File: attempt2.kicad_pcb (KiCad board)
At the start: 4 copper layers, 88.5 x 54.4 mm, 60 parts, among them J1 Conn_ARM_JTAG_SWD_10, J4 USB_C_Receptacle_USB2.0_14P, J5 SIM_Card, SW1 SW_Push, SW4 SW_Push, U3 MCP73831T-2ACI_OT, U4 NRF9151-LACA-R7, U5 MAX2686LEWS_, U7 CP2102N-A02-GQFN24R

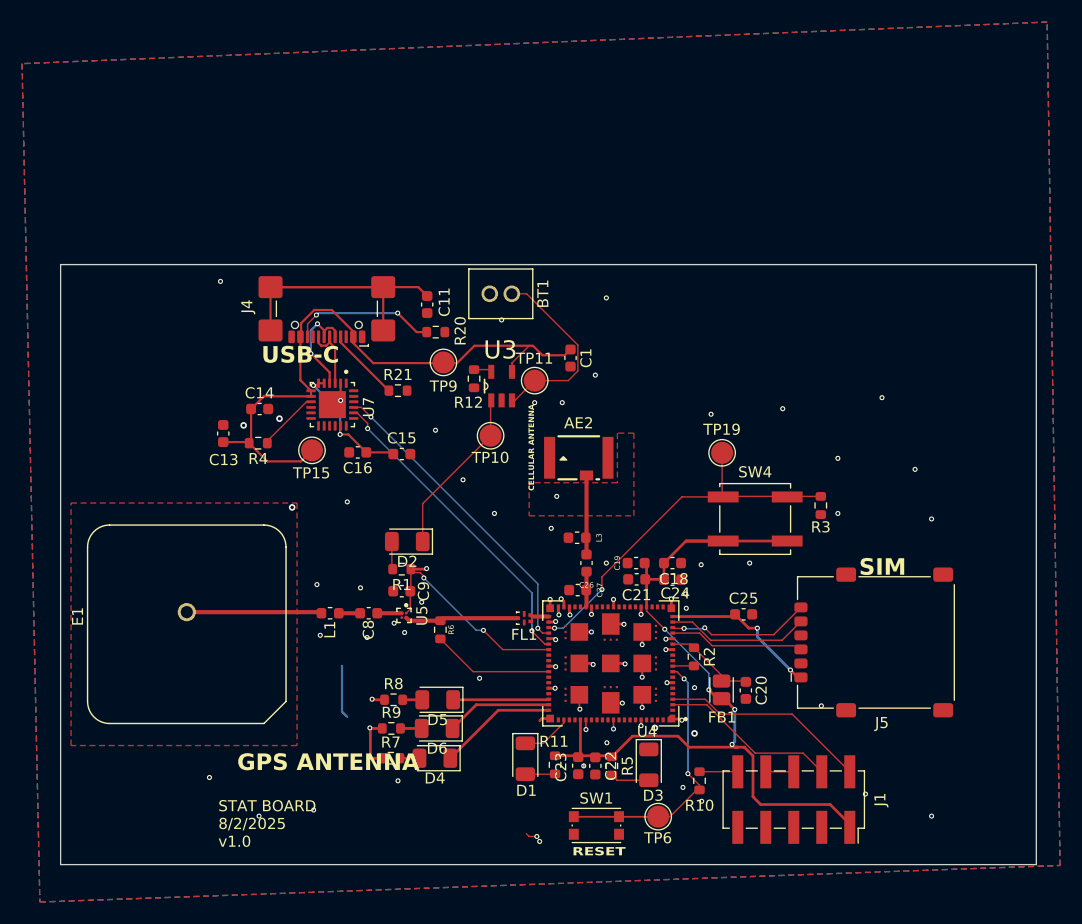
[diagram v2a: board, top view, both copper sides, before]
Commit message: moved some ground pins
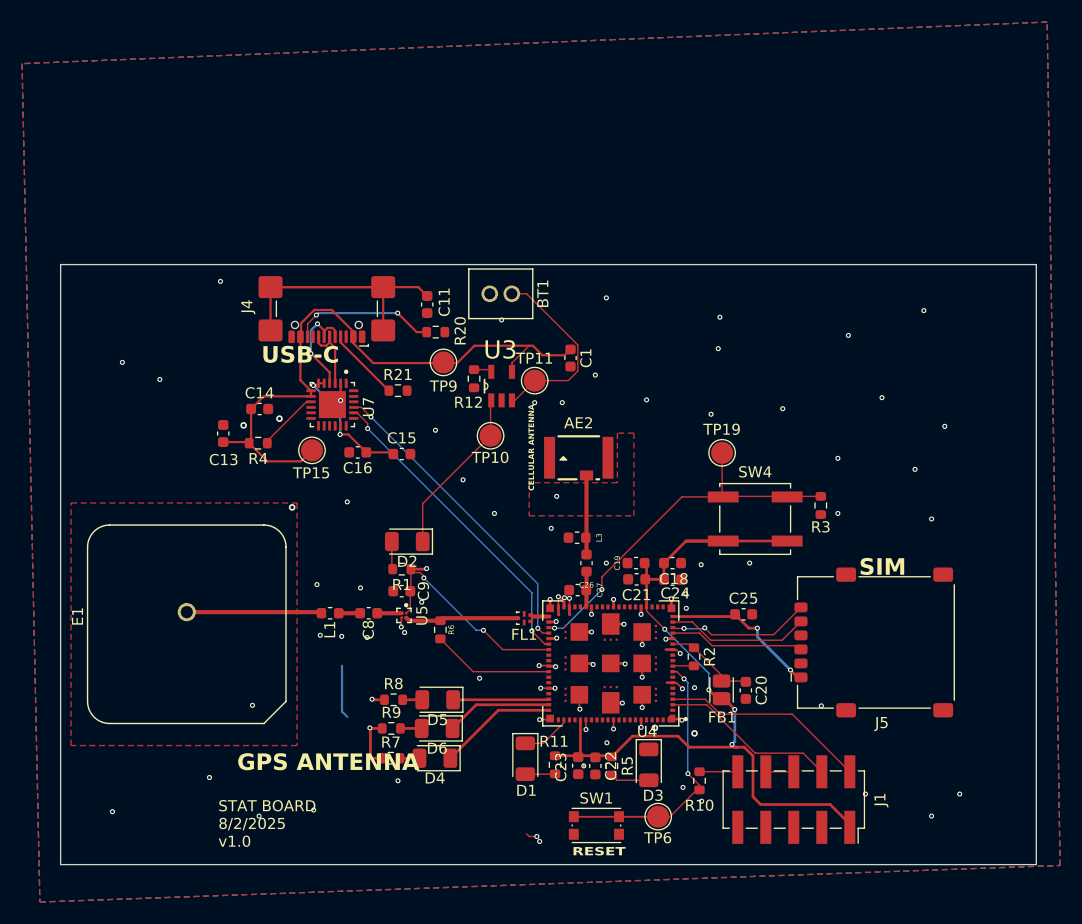
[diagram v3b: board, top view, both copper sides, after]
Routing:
- net GND: track 34.4 -> 43.7 mm, vias 80 -> 95
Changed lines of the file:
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@@
-	)
-	(segment
-		(start 132.15 128.15)
-		(end 131.95 128.35)
-		(width 0.25)
-		(layer "F.Cu")
-		(net 1)
 	)
 	(segment
@@
 	)
 	(segment
+		(start 132.675 120.85)
+		(end 133.5 120.85)
+		(width 0.15)
+		(layer "F.Cu")
+		(net 1)
+	)
+	(segment
+		(start 143.925 124.9)
+		(end 144.35 124.9)
+		(width 0.15)
+		(layer "F.Cu")
+		(net 1)
+	)
+	(segment
 		(start 135.55 120.3)
 		(end 136.65 120.3)
@@
 	)
 	(segment
+		(start 132.775 128.25)
+		(end 131.95 128.25)
+		(width 0.15)
+		(layer "F.Cu")
+		(net 1)
+	)
+	(segment
 		(start 132.775 120.9)
 		(end 133.3 120.9)
@@
 	)
 	(segment
+		(start 141.15 128.125)
+		(end 141.15 128.95)
+		(width 0.15)
+		(layer "F.Cu")
+		(net 1)
+	)
+	(segment
 		(start 136.7 123.15)
 		(end 136.8 123.25)
@@
 	)
 	(segment
+		(start 144.35 124.9)
+		(end 144.9 125.45)
+		(width 0.15)
+		(layer "F.Cu")
+		(net 1)
+	)
+	(segment
 		(start 113.525 99.675)
 		(end 113.9 99.3)
 		(width 0.2)
+		(layer "F.Cu")
+		(net 1)
+	)
+	(segment
+		(start 144.35 121.9)
+		(end 144.7 122.25)
+		(width 0.15)
 		(layer "F.Cu")
 		(net 1)
@@
 	)
 	(segment
+		(start 133.65 117.925)
+		(end 133.65 117.1)
+		(width 0.15)
+		(layer "F.Cu")
+		(net 1)
+	)
+	(segment
+		(start 132.625 119.35)
+		(end 133.45 119.35)
+		(width 0.15)
+		(layer "F.Cu")
+		(net 1)
+	)
+	(segment
 		(start 138.4 123.15)
 		(end 139.65 123.15)
@@
 	)
 	(segment
+		(start 132.725 123.35)
+		(end 131.9 123.35)
+		(width 0.15)
+		(layer "F.Cu")
+		(net 1)
+	)
+	(segment
 		(start 135.55 123.15)
 		(end 136.7 123.15)
@@
 		(end 133.4 121)
 		(width 0.25)
+		(layer "F.Cu")
+		(net 1)
+	)
+	(segment
+		(start 134.2 118.025)
+		(end 134.2 117.2)
+		(width 0.15)
 		(layer "F.Cu")
 		(net 1)
@@
 	)
 	(segment
+		(start 132.875 125.4)
+		(end 132.05 125.4)
+		(width 0.15)
+		(layer "F.Cu")
+		(net 1)
+	)
+	(segment
 		(start 133.65 118.025)
 		(end 133.65 118.7)
@@
 		(end 139.575 119.575)
 		(width 0.25)
+		(layer "F.Cu")
+		(net 1)
+	)
+	(segment
+		(start 119.4 119.025)
+		(end 119.4 119.85)
+		(width 0.15)
 		(layer "F.Cu")
 		(net 1)
@@
 	)
 	(segment
+		(start 143.975 121.9)
+		(end 144.35 121.9)
+		(width 0.15)
+		(layer "F.Cu")
+		(net 1)
+	)
+	(segment
 		(start 138.4 126.725)
 		(end 139.425 126.725)
@@
 	)
 	(segment
+		(start 134.65 118.075)
+		(end 134.65 117.25)
+		(width 0.15)
+		(layer "F.Cu")
+		(net 1)
+	)
+	(segment
 		(start 139.425 126.725)
 		(end 139.45 126.75)
@@
 	)
 	(segment
-		(start 132.9 128.15)
-		(end 132.15 128.15)
-		(width 0.25)
-		(layer "F.Cu")
-		(net 1)
-	)
-	(segment
 		(start 133.35 119.4)
 		(end 133.4 119.35)
@@
 	)
 	(via
-		(at 141.15 128.8)
-		(size 0.4572)
-		(drill 0.254)
-		(layers "F.Cu" "B.Cu")
+		(at 148.15 94.6)
+		(size 0.4572)
+		(drill 0.254)
+		(layers "F.Cu" "B.Cu")
+		(free yes)
+		(net 1)
+	)
+	(via
+		(at 168.7 101.65)
+		(size 0.4572)
+		(drill 0.254)
+		(layers "F.Cu" "B.Cu")
+		(free yes)
 		(net 1)
 	)
@@
 	)
 	(via
+		(at 132.05 125.4)
+		(size 0.4572)
+		(drill 0.254)
+		(layers "F.Cu" "B.Cu")
+		(net 1)
+	)
+	(via
+		(at 119.4 119.85)
+		(size 0.4572)
+		(drill 0.254)
+		(layers "F.Cu" "B.Cu")
+		(net 1)
+	)
+	(via
+		(at 144.9 125.45)
+		(size 0.4572)
+		(drill 0.254)
+		(layers "F.Cu" "B.Cu")
+		(net 1)
+	)
+	(via
 		(at 146.65 135.65)
 		(size 0.4572)
@@
 	)
 	(via
-		(at 133.4 119.35)
-		(size 0.4572)
-		(drill 0.254)
-		(layers "F.Cu" "B.Cu")
-		(net 1)
-	)
-	(via
-		(at 143.4 121.9)
-		(size 0.4572)
-		(drill 0.254)
-		(layers "F.Cu" "B.Cu")
-		(net 1)
-	)
-	(via
 		(at 143.9 117.3)
 		(size 0.4572)
@@
 	)
 	(via
-		(at 133.4 121)
+		(at 141.15 128.95)
+		(size 0.4572)
+		(drill 0.254)
+		(layers "F.Cu" "B.Cu")
+		(net 1)
+	)
+	(via
+		(at 133.45 119.35)
 		(size 0.4572)
 		(drill 0.254)
@@
 	)
 	(via
+		(at 134.2 117.2)
+		(size 0.4572)
+		(drill 0.254)
+		(layers "F.Cu" "B.Cu")
+		(net 1)
+	)
+	(via
 		(at 132.9 117.35)
 		(size 0.4572)
@@
 	)
 	(via
-		(at 133.7 118.75)
-		(size 0.4572)
-		(drill 0.254)
-		(layers "F.Cu" "B.Cu")
+		(at 105.9 126.95)
+		(size 0.4572)
+		(drill 0.254)
+		(layers "F.Cu" "B.Cu")
+		(free yes)
+		(net 1)
+	)
+	(via
+		(at 114 120.7)
+		(size 0.4572)
+		(drill 0.254)
+		(layers "F.Cu" "B.Cu")
+		(free yes)
+		(net 1)
+	)
+	(via
+		(at 133.65 117.1)
+		(size 0.4572)
+		(drill 0.254)
+		(layers "F.Cu" "B.Cu")
+		(net 1)
+	)
+	(via
+		(at 94.1 95.85)
+		(size 0.4572)
+		(drill 0.254)
+		(layers "F.Cu" "B.Cu")
+		(free yes)
 		(net 1)
 	)
@@
 	)
 	(via
-		(at 133.9 117.3)
-		(size 0.4572)
-		(drill 0.254)
-		(layers "F.Cu" "B.Cu")
-		(net 1)
-	)
-	(via
 		(at 159 104.55)
 		(size 0.4572)
@@
 	)
 	(via
-		(at 134.7 118.75)
-		(size 0.4572)
-		(drill 0.254)
-		(layers "F.Cu" "B.Cu")
-		(net 1)
-	)
-	(via
-		(at 118.75 119.5)
+		(at 148.3 91.75)
+		(size 0.4572)
+		(drill 0.254)
+		(layers "F.Cu" "B.Cu")
+		(free yes)
+		(net 1)
+	)
+	(via
+		(at 93.2 136.6)
 		(size 0.4572)
 		(drill 0.254)
@@
 	)
 	(via
+		(at 134.65 117.25)
+		(size 0.4572)
+		(drill 0.254)
+		(layers "F.Cu" "B.Cu")
+		(net 1)
+	)
+	(via
 		(at 103 88.5)
 		(size 0.4572)
@@
 	)
 	(via
+		(at 141.65 99.25)
+		(size 0.4572)
+		(drill 0.254)
+		(layers "F.Cu" "B.Cu")
+		(free yes)
+		(net 1)
+	)
+	(via
 		(at 138.65 129.1)
 		(size 0.4572)
@@
 	)
 	(via
-		(at 143.5 124.9)
-		(size 0.4572)
-		(drill 0.254)
-		(layers "F.Cu" "B.Cu")
+		(at 131.9 123.35)
+		(size 0.4572)
+		(drill 0.254)
+		(layers "F.Cu" "B.Cu")
+		(net 1)
+	)
+	(via
+		(at 159.95 93.4)
+		(size 0.4572)
+		(drill 0.254)
+		(layers "F.Cu" "B.Cu")
+		(free yes)
 		(net 1)
 	)
@@
 	)
 	(via
+		(at 144.7 122.25)
+		(size 0.4572)
+		(drill 0.254)
+		(layers "F.Cu" "B.Cu")
+		(net 1)
+	)
+	(via
 		(at 127.85 109.55)
 		(size 0.4572)
@@
 	)
 	(via
+		(at 170.05 135)
+		(size 0.4572)
+		(drill 0.254)
+		(layers "F.Cu" "B.Cu")
+		(free yes)
+		(net 1)
+	)
+	(via
 		(at 105.1 101.56)
 		(size 0.6)
@@
 	)
 	(via
+		(at 133.5 120.85)
+		(size 0.4572)
+		(drill 0.254)
+		(layers "F.Cu" "B.Cu")
+		(net 1)
+	)
+	(via
 		(at 154 100.05)
+		(size 0.4572)
+		(drill 0.254)
+		(layers "F.Cu" "B.Cu")
+		(free yes)
+		(net 1)
+	)
+	(via
+		(at 166.8 91.15)
 		(size 0.4572)
 		(drill 0.254)
@@
 	)
 	(via
+		(at 131.95 128.25)
+		(size 0.4572)
+		(drill 0.254)
+		(layers "F.Cu" "B.Cu")
+		(net 1)
+	)
+	(via
 		(at 131.7 138.85)
 		(size 0.4572)
@@
 	(via
 		(at 121.25 117.6)
+		(size 0.4572)
+		(drill 0.254)
+		(layers "F.Cu" "B.Cu")
+		(free yes)
+		(net 1)
+	)
+	(via
+		(at 97.5 97.4)
 		(size 0.4572)
 		(drill 0.254)
@@
 	)
 	(segment
+		(start 130.125 114.275)
+		(end 116.65 100.8)
+		(width 0.127)
+		(layer "B.Cu")
+		(net 42)
+	)
+	(segment
 		(start 131.783851 115.933851)
-		(end 116.65 100.8)
+		(end 130.125 114.275)
 		(width 0.127)
 		(layer "B.Cu")

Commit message: worked with andrew on a few adjustments
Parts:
- removed TP10: TestPoint, TestPoint:TestPoint_Pad_D2.0mm
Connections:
- D2 pad 1: Net-(D2-K) -> CHARGE_STAT
- R1 pad 1: CHARGE_STAT -> +3V8
- U3 pad 1: Net-(D2-K) -> CHARGE_STAT
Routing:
- net Net-(D2-K): track 15.1 -> 0.00 mm
- net CHARGE_STAT: track 15.2 -> 30.4 mm
- net STATUS_LED: track 4.60 -> 5.20 mm
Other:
- board text added: "STAT BOARD 9/17/2025 v1.0"
- board text removed: "STAT BOARD 8/2/2025 v1.0"
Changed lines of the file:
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@@
 	(net 91 "+3V8")
 	(net 92 "Net-(E1-Pad1)")
-	(net 93 "Net-(D2-K)")
 	(footprint "Resistor_SMD:R_0603_1608Metric"
 		(layer "F.Cu")
@@
 	(footprint "TestPoint:TestPoint_Pad_D2.0mm"
 		(layer "F.Cu")
-		(at 127.5 102.5 180)
-		(descr "SMD pad as test Point, diameter 2.0mm")
-		(tags "test point SMD pad")
-		(property "Reference" "TP10"
-			(at 0 -1.998 0)
-			(layer "F.SilkS")
-			(effects
-				(font
-					(size 1 1)
-					(thickness 0.15)
-				)
-			)
-		)
-		(property "Value" "TestPoint"
-			(at 0 2.05 0)
-			(layer "F.Fab")
-			(effects
-				(font
-					(size 1 1)
-					(thickness 0.15)
-				)
-			)
-		)
-		(property "Datasheet" ""
-			(at 0 0 180)
-			(unlocked yes)
-			(layer "F.Fab")
-			(hide yes)
-			(effects
-				(font
-					(size 1.27 1.27)
-					(thickness 0.15)
-				)
-			)
-		)
-		(property "Description" "test point"
-			(at 0 0 180)
-			(unlocked yes)
-			(layer "F.Fab")
-			(hide yes)
-			(effects
-				(font
-					(size 1.27 1.27)
-					(thickness 0.15)
-				)
-			)
-		)
-		(property ki_fp_filters "Pin* Test*")
-		(sheetname "/")
-		(sheetfile "attempt2.kicad_sch")
-		(attr exclude_from_pos_files)
-		(fp_circle
-			(center 0 0)
-			(end 0 1.2)
-			(stroke
-				(width 0.12)
-				(type solid)
-			)
-			(fill no)
-			(layer "F.SilkS")
-		)
-		(fp_circle
-			(center 0 0)
-			(end 1.5 0)
-			(stroke
-				(width 0.05)
-				(type solid)
-			)
-			(fill no)
-			(layer "F.CrtYd")
-		)
-		(fp_text user "${REFERENCE}"
-			(at 0 -2 0)
-			(layer "F.Fab")
-			(effects
-				(font
-					(size 1 1)
-					(thickness 0.15)
-				)
-			)
-		)
-		(pad "1" smd circle
-			(at 0 0 180)
-			(size 2 2)
-			(layers "F.Cu" "F.Mask")
-			(net 93 "Net-(D2-K)")
-			(pinfunction "1")
-			(pintype "passive")
-		)
-		(embedded_fonts no)
-	)
-	(footprint "TestPoint:TestPoint_Pad_D2.0mm"
-		(layer "F.Cu")
 		(at 131.5 97.5 90)
 		(descr "SMD pad as test Point, diameter 2.0mm")
@@
 			(layers "F.Cu" "F.Mask" "F.Paste")
 			(roundrect_rratio 0.2)
-			(net 93 "Net-(D2-K)")
+			(net 14 "CHARGE_STAT")
 			(pinfunction "K")
 			(pintype "passive")
@@
 			(layers "F.Cu" "F.Mask" "F.Paste")
 			(roundrect_rratio 0.25)
-			(net 14 "CHARGE_STAT")
+			(net 91 "+3V8")
 			(pintype "passive")
 		)
@@
 			(size 1.27 0.5588)
 			(layers "F.Cu" "F.Mask" "F.Paste")
-			(net 93 "Net-(D2-K)")
+			(net 14 "CHARGE_STAT")
 			(pinfunction "STAT")
 			(pintype "output")
@@
 		(layer "Edge.Cuts")
 	)
-	(gr_text "STAT BOARD\n8/2/2025\nv1.0"
+	(gr_text "STAT BOARD\n9/17/2025\nv1.0"
 		(at 102.8 139.9 0)
 		(layer "F.SilkS")
@@
 	)
 	(gr_text "CELLULAR ANTENNA"
-		(at 131.5 107.5 90)
+		(at 131.35 109.3 90)
 		(layer "F.SilkS")
 		(effects
@@
 	)
 	(segment
-		(start 134.15 128.533)
-		(end 134.15 128.275)
+		(start 133.3 130.4)
+		(end 130.65 130.4)
 		(width 0.127)
 		(layer "F.Cu")
@@
 	)
 	(segment
-		(start 132.283 130.4)
-		(end 134.15 128.533)
+		(start 134.15 128.275)
+		(end 134.15 129.55)
 		(width 0.127)
 		(layer "F.Cu")
@@
 	)
 	(segment
-		(start 130.65 130.4)
-		(end 132.283 130.4)
+		(start 134.2 128.325)
+		(end 134.15 128.275)
 		(width 0.127)
 		(layer "F.Cu")
@@
 	)
 	(segment
-		(start 134.2 128.325)
-		(end 134.15 128.275)
+		(start 134.15 129.55)
+		(end 133.3 130.4)
 		(width 0.127)
 		(layer "F.Cu")
@@
 	)
 	(segment
+		(start 127.5 102.5)
+		(end 121.34375 108.65625)
+		(width 0.127)
+		(layer "F.Cu")
+		(net 14)
+	)
+	(segment
 		(start 121.45 115.25)
 		(end 121.1165 114.9165)
@@
 	)
 	(segment
+		(start 127.5 102.5)
+		(end 127.5 99.3556)
+		(width 0.127)
+		(layer "F.Cu")
+		(net 14)
+	)
+	(segment
+		(start 127.5 99.3556)
+		(end 127.5602 99.2954)
+		(width 0.127)
+		(layer "F.Cu")
+		(net 14)
+	)
+	(segment
+		(start 121.34375 108.65625)
+		(end 121.34375 111.845)
+		(width 0.127)
+		(layer "F.Cu")
+		(net 14)
+	)
+	(segment
 		(start 128.6 121.9)
 		(end 126.85 120.15)
@@
 		(net 92)
 	)
-	(segment
-		(start 127.5 102.5)
-		(end 121.34375 108.65625)
-		(width 0.127)
-		(layer "F.Cu")
-		(net 93)
-	)
-	(segment
-		(start 127.5 102.5)
-		(end 127.5 99.3556)
-		(width 0.127)
-		(layer "F.Cu")
-		(net 93)
-	)
-	(segment
-		(start 127.5 99.3556)
-		(end 127.5602 99.2954)
-		(width 0.127)
-		(layer "F.Cu")
-		(net 93)
-	)
-	(segment
-		(start 121.34375 108.65625)
-		(end 121.34375 111.845)
-		(width 0.127)
-		(layer "F.Cu")
-		(net 93)
-	)
-	(zone
-		(net 1)
-		(net_name "GND")
-		(layer "F.Cu")
-		(hatch edge 0.5)
-		(priority 3)
-		(connect_pads
-			(clearance 0.2)
-		)
-		(min_thickness 0.25)
-		(filled_areas_thickness no)
-		(fill yes
-			(thermal_gap 0.5)
-			(thermal_bridge_width 0.5)
-		)
-		(polygon
-			(pts
-				(xy 140.5 109.7625) (xy 140.5 102.2625) (xy 139 102.2625) (xy 139 106.7625) (xy 131 106.7625) (xy 131 109.7625)
-			)
-		)
-	)
-	(zone
-		(net 1)
-		(net_name "GND")
-		(layer "F.Cu")
-		(hatch edge 0.5)
-		(priority 2)
-		(connect_pads
-			(clearance 0.2)
-		)
-		(min_thickness 0.25)
-		(filled_areas_thickness no)
-		(fill yes
-			(thermal_gap 0.5)
-			(thermal_bridge_width 0.5)
-		)
-		(polygon
-			(pts
-				(xy 109.94375 108.6) (xy 109.94375 130.6) (xy 89.44375 130.6) (xy 89.44375 108.6)
-			)
-		)
-	)
 	(zone
 		(net 1)
 		(net_name "GND")
+		(locked yes)
 		(layers "F.Cu" "B.Cu" "In1.Cu" "In2.Cu")
 		(hatch none 0.5)

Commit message: changes made with andrew
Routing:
- net CHARGE_STAT: track 30.4 -> 34.3 mm
- net GND: track 43.7 -> 42.6 mm, vias 95 -> 94
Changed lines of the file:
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@@
 		(tags "capacitor")
 		(property "Reference" "C9"
-			(at -2 0 90)
+			(at -4.75625 2.6 90)
 			(layer "F.SilkS")
 			(effects
@@
 		(at 138.4 123.15 180)
 		(property "Reference" "U4"
-			(at -3.3 -6.2 0)
+			(at -1.35 -6.5 0)
 			(layer "F.SilkS")
 			(effects
@@
 		(tags "tactile switch kmr2")
 		(property "Reference" "SW1"
-			(at 0 -2.45 0)
+			(at -3.6 -0.05 90)
 			(layer "F.SilkS")
 			(effects
@@
 		(tags "capacitor")
 		(property "Reference" "C22"
-			(at 0 -1.43 90)
+			(at -2.15 0.7 180)
 			(layer "F.SilkS")
 			(effects
@@
 		(tags "capacitor")
 		(property "Reference" "C23"
-			(at 0.14058 1.55 90)
+			(at 2.025 -0.05 180)
 			(layer "F.SilkS")
 			(effects
@@
 		(tags "capacitor")
 		(property "Reference" "C8"
-			(at 0 1.5 90)
+			(at 0 1.5 180)
 			(layer "F.SilkS")
 			(effects
@@
 		(tags "LED")
 		(property "Reference" "D3"
-			(at 2.8 -0.4 180)
+			(at -0.3425 -2.05 270)
 			(layer "F.SilkS")
 			(effects
@@
 		(tags "inductor")
 		(property "Reference" "L1"
-			(at 0 -1.5 90)
+			(at 0 -1.5 180)
 			(layer "F.SilkS")
 			(effects
@@
 		(tags "LED")
 		(property "Reference" "D2"
-			(at 0 -1.83 0)
+			(at 0.49375 2.1 0)
 			(layer "F.SilkS")
 			(effects
@@
 		(tags "resistor")
 		(property "Reference" "R1"
-			(at 0 -1.43 0)
+			(at 2.49375 0.05 90)
 			(layer "F.SilkS")
 			(effects
@@
 	)
 	(gr_text "STAT BOARD\n9/17/2025\nv1.0"
-		(at 102.8 139.9 0)
+		(at 91.15 138.45 0)
 		(layer "F.SilkS")
 		(effects
@@
 	)
 	(gr_text "CELLULAR ANTENNA"
-		(at 131.35 109.3 90)
+		(at 131.55 107.1 90)
 		(layer "F.SilkS")
 		(effects
@@
 	)
 	(gr_text "GPS ANTENNA"
-		(at 104.5 133 0)
+		(at 90.7 132.75 0)
 		(layer "F.SilkS")
 		(effects
@@
 	)
 	(segment
-		(start 131.7 138.85)
-		(end 131 138.85)
-		(width 0.127)
-		(layer "F.Cu")
-		(net 1)
-	)
-	(segment
 		(start 113.9 98.925)
 		(end 113.9 97.74)
@@
 	)
 	(segment
-		(start 131 138.85)
-		(end 130.75 138.6)
-		(width 0.127)
-		(layer "F.Cu")
-		(net 1)
-	)
-	(segment
 		(start 134.15 117.55)
 		(end 133.9 117.3)
@@
 	)
 	(via
-		(at 131.5 99.5)
-		(size 0.4572)
-		(drill 0.254)
-		(layers "F.Cu" "B.Cu")
-		(free yes)
-		(net 1)
-	)
-	(via
 		(at 144.85 128.3)
 		(size 0.4572)
@@
 	)
 	(segment
+		(start 122.1201 114.7299)
+		(end 121.45 115.4)
+		(width 0.127)
+		(layer "F.Cu")
+		(net 14)
+	)
+	(segment
 		(start 121.1165 114.9165)
 		(end 120.52375 114.9165)
@@
 	)
 	(segment
+		(start 122.1201 112.87635)
+		(end 122.1201 114.7299)
+		(width 0.127)
+		(layer "F.Cu")
+		(net 14)
+	)
+	(segment
 		(start 128.6 121.9)
 		(end 126.85 120.15)
 		(width 0.127)
 		(layer "F.Cu")
+		(net 14)
+	)
+	(segment
+		(start 121.34375 112.1)
+		(end 122.1201 112.87635)
+		(width 0.127)
+		(layer "F.Cu")

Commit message: unno
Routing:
- net GND: track 42.6 -> 37.8 mm
- net CHARGE_STAT: track 34.3 -> 31.7 mm
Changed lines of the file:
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@@
 		(tags "capacitor")
 		(property "Reference" "C18"
-			(at 0.125 1.45 0)
+			(at 0.14058 -1.8 0)
 			(layer "F.SilkS")
 			(effects
@@
 		(tags "capacitor")
 		(property "Reference" "C22"
-			(at -2.15 0.7 180)
+			(at -2.15 0 180)
 			(layer "F.SilkS")
 			(effects
@@
 		(tags "capacitor")
 		(property "Reference" "C21"
-			(at 0 -1.43 0)
+			(at 0 -1.375 0)
 			(layer "F.SilkS")
 			(effects
@@
 		(tags "capacitor")
 		(property "Reference" "C19"
-			(at 1.7 0 90)
+			(at 0 1.8 180)
 			(layer "F.SilkS")
 			(effects
 				(font
-					(size 0.5 0.5)
-					(thickness 0.0625)
+					(size 1 1)
+					(thickness 0.125)
 				)
 			)
@@
 	)
 	(segment
-		(start 114.022778 123.375)
-		(end 114.022778 127.522778)
-		(width 0.2)
-		(layer "B.Cu")
-		(net 1)
-	)
-	(segment
-		(start 114.022778 127.522778)
-		(end 114.5 128)
-		(width 0.2)
-		(layer "B.Cu")
-		(net 1)
-	)
-	(segment
 		(start 116.860001 95.91)
 		(end 124.465 95.91)
@@
 	)
 	(segment
-		(start 121.45 115.25)
-		(end 121.1165 114.9165)
+		(start 122.75 112.15)
+		(end 122.7 112.1)
 		(width 0.127)
 		(layer "F.Cu")
@@
 	(segment
 		(start 132.775 121.9)
-		(end 128.6 121.9)
-		(width 0.127)
-		(layer "F.Cu")
-		(net 14)
-	)
-	(segment
-		(start 122.1201 114.7299)
-		(end 121.45 115.4)
-		(width 0.127)
-		(layer "F.Cu")
-		(net 14)
-	)
-	(segment
-		(start 121.1165 114.9165)
-		(end 120.52375 114.9165)
-		(width 0.127)
-		(layer "F.Cu")
-		(net 14)
-	)
-	(segment
-		(start 121.45 115.4)
-		(end 121.45 115.25)
+		(end 130.6251 121.9)
 		(width 0.127)
 		(layer "F.Cu")
@@
 	)
 	(segment
-		(start 122.1201 112.87635)
-		(end 122.1201 114.7299)
-		(width 0.127)
-		(layer "F.Cu")
-		(net 14)
-	)
-	(segment
-		(start 128.6 121.9)
-		(end 126.85 120.15)
+		(start 122.7 112.1)
+		(end 121.34375 112.1)
 		(width 0.127)
 		(layer "F.Cu")
@@
 	)
 	(segment
-		(start 121.34375 112.1)
-		(end 122.1201 112.87635)
+		(start 130.6251 121.9)
+		(end 128.8 120.0749)
 		(width 0.127)
 		(layer "F.Cu")
@@
 	)
 	(via
-		(at 121.45 115.4)
+		(at 122.75 112.15)
 		(size 0.4572)
 		(drill 0.254)
@@
 	)
 	(via
-		(at 126.85 120.15)
+		(at 128.8 120.0749)
 		(size 0.4572)
 		(drill 0.254)
@@
 	)
 	(segment
-		(start 126.85 120.15)
-		(end 126.2 120.15)
+		(start 128.8 118.2)
+		(end 122.75 112.15)
 		(width 0.127)
 		(layer "B.Cu")
@@
 	)
 	(segment
-		(start 126.2 120.15)
-		(end 121.45 115.4)
+		(start 128.8 120.0749)
+		(end 128.8 118.2)
 		(width 0.127)
 		(layer "B.Cu")
